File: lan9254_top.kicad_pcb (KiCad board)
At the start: 4 copper layers, 60 x 100 mm, 100 parts, among them J1 BEL_0845_2G1T_H5, J2 BNC, J3 BNC, SW1 SW_DIP_x08, U1 lan9254, U2 74LVC1G06, U3 74LVC1G06, U4 74LVC1G06, U5 PCA9306, U6 74LVC1G06, U7 74LVC2T45DC, U8 24AA0x, U9 74LVC2T45DC, X1 FNETHE025

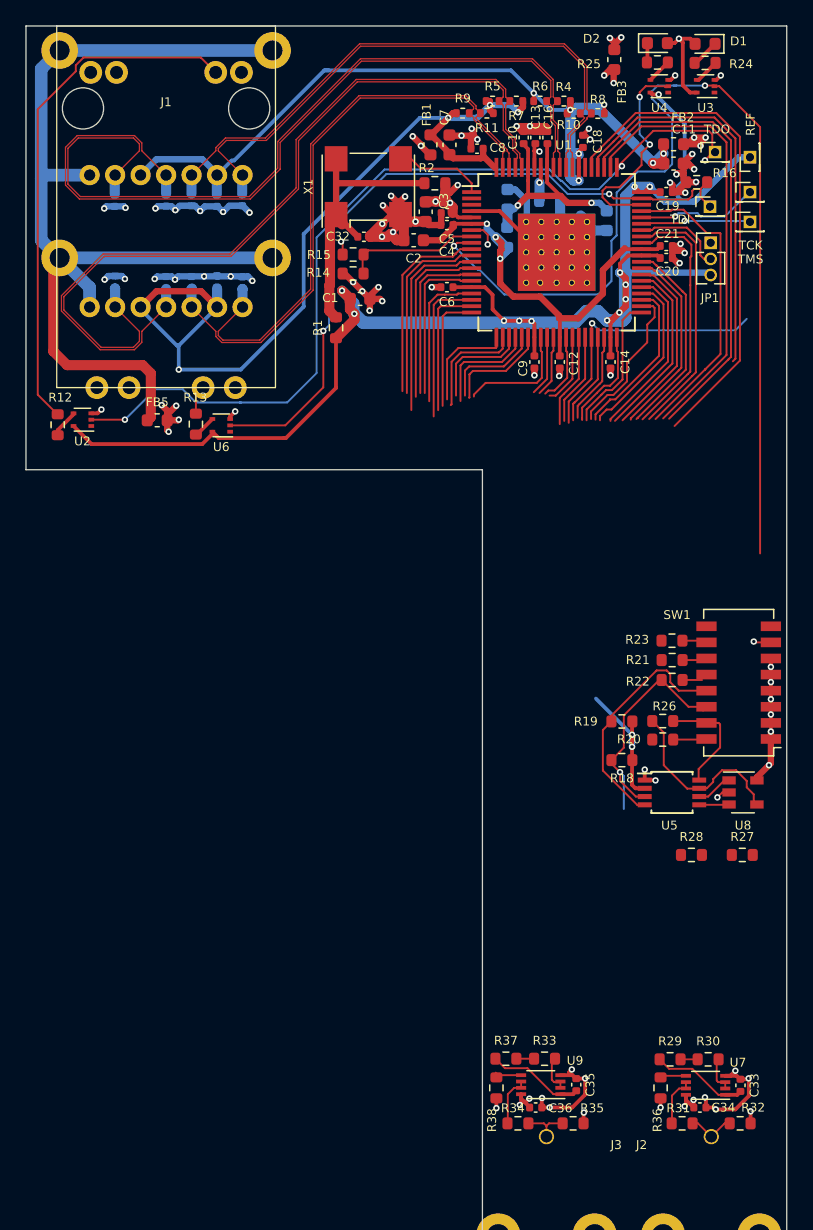
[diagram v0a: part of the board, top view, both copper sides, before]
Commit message: reannotated for merging with te0715 development board
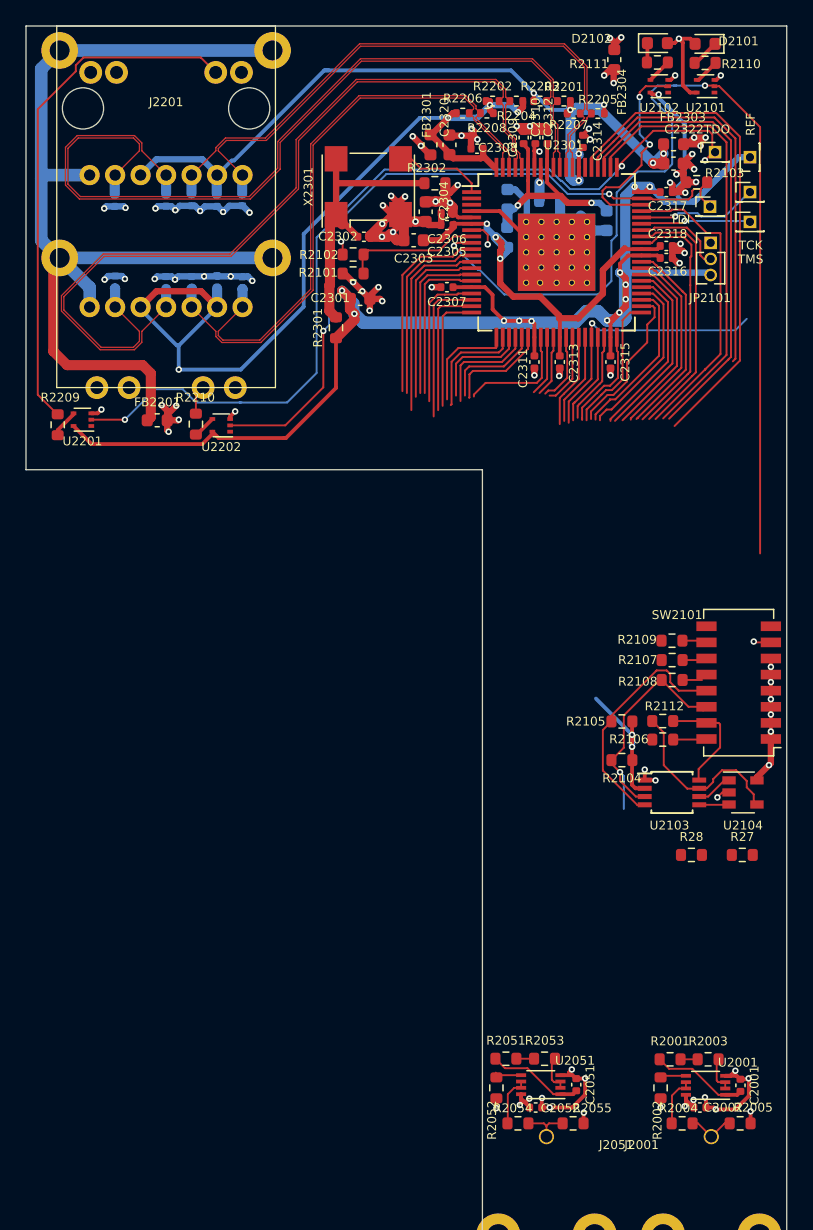
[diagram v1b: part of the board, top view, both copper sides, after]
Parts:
- renumbered C33 to C2001, C34 to C2002, C35 to C2051, C36 to C2052, C22 to C2201, C23 to C2202, C24 to C2203, C25 to C2204, C26 to C2205, C27 to C2206, C28 to C2207, C29 to C2208, C30 to C2209, C31 to C2210, C1 to C2301, C32 to C2302, C2 to C2303, C3 to C2304, C4 to C2305, C5 to C2306, C6 to C2307, C8 to C2308, C10 to C2309, C13 to C2310, C9 to C2311, C16 to C2312, C12 to C2313, C18 to C2314, C14 to C2315, C20 to C2316, C19 to C2317, C21 to C2318, C15 to C2319, C7 to C2320, C17 to C2321, C11 to C2322, D1 to D2101, D2 to D2102, FB5 to FB2201, FB1 to FB2301, FB4 to FB2302, FB2 to FB2303, FB3 to FB2304, J2 to J2001, J3 to J2051, J1 to J2201, JP1 to JP2101, R29 to R2001, R36 to R2002, R30 to R2003, R31 to R2004, R32 to R2005, R37 to R2051, R38 to R2052, R33 to R2053, R34 to R2054, R35 to R2055, R14 to R2101, R15 to R2102, R16 to R2103, R18 to R2104, R19 to R2105, R20 to R2106, R21 to R2107, R22 to R2108, R23 to R2109, R24 to R2110, R25 to R2111, R26 to R2112, R4 to R2201, R5 to R2202, R6 to R2203, R7 to R2204, R8 to R2205, R9 to R2206, R10 to R2207, R11 to R2208, R12 to R2209, R13 to R2210, R1 to R2301, R2 to R2302, R3 to R2303, SW1 to SW2101, TP1 to TP2301, TP2 to TP2302, TP3 to TP2303, TP4 to TP2304, TP5 to TP2305, U7 to U2001, U9 to U2051, U3 to U2101, U4 to U2102, U5 to U2103, U8 to U2104, U2 to U2201, U6 to U2202, U1 to U2301, X1 to X2301

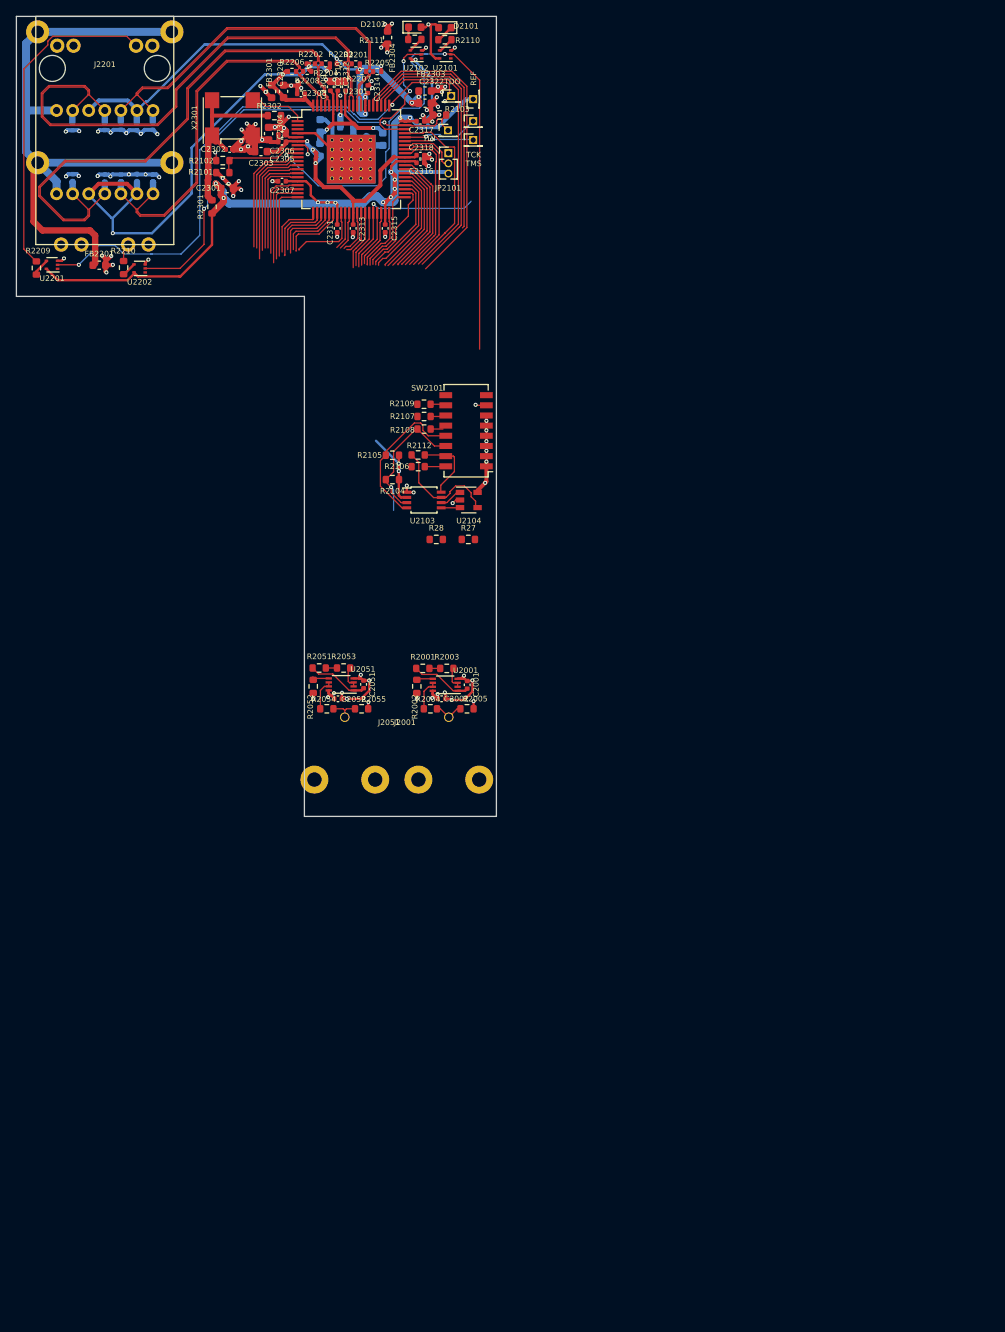
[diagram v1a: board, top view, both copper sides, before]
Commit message: moved PCB to not overlap with te0715 base board
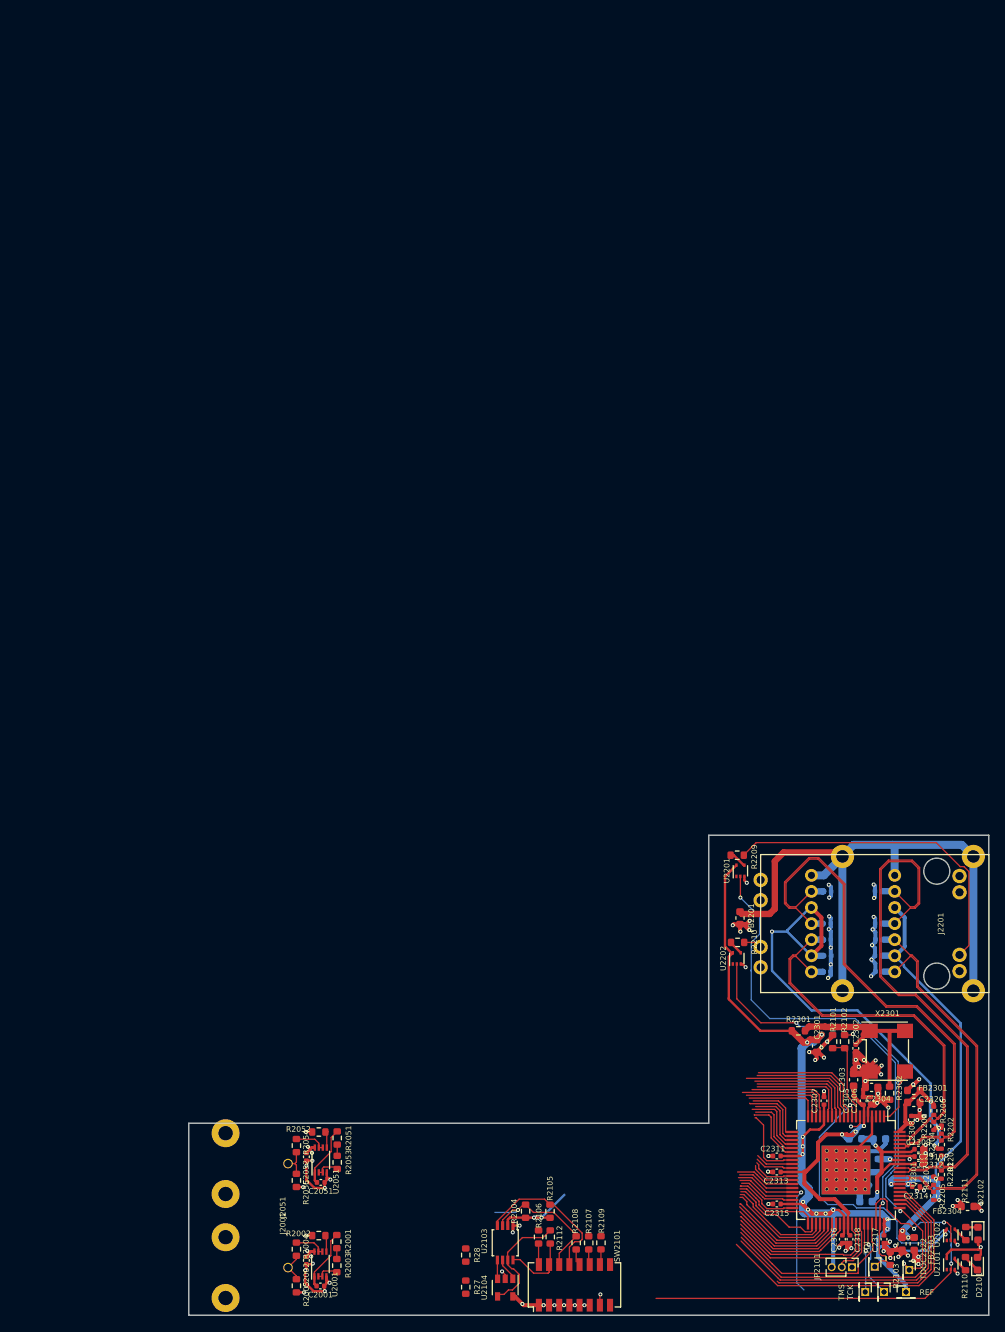
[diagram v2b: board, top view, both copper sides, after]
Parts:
- moved D2101 168.2 mm to (250.1, 195.9), turned to 90 degrees
- moved D2102 166.4 mm to (250.2, 192.2), turned to 270 degrees
- moved R2110 166.3 mm to (248.6, 195.9), turned to 270 degrees
- moved R2111 164.4 mm to (248.7, 192.2), turned to 270 degrees
- moved U2101 163.9 mm to (246.8, 195.9), turned to 90 degrees
- moved FB2304 163.1 mm to (248.9, 188.8), turned to 180 degrees
- moved U2102 162.0 mm to (246.8, 192.3), turned to 90 degrees
- moved TP2305 158.6 mm to (241.2, 199.4), turned to 0 degrees
- moved TP2301 157.5 mm to (241.6, 196.7), turned to 270 degrees
- moved R2201 157.0 mm to (245.6, 184.8), turned to 90 degrees
- moved R2205 156.8 mm to (244.7, 187.4), turned to 90 degrees
- moved FB2303 156.5 mm to (242.2, 193.4), turned to 90 degrees
- moved R2203 156.2 mm to (245.6, 182.9), turned to 270 degrees
- moved R2207 156.0 mm to (244.7, 185.6), turned to 270 degrees
- moved R2204 155.5 mm to (245.6, 181.0), turned to 90 degrees
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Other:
- board size 60 x 100 mm -> 100 x 60 mm

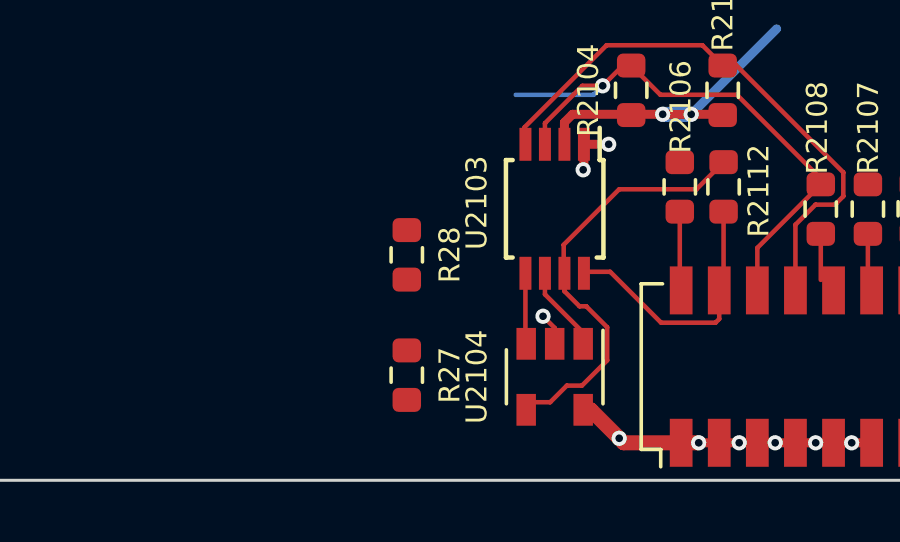
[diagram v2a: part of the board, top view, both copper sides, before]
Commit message: reannotated top-module and updated PCB (prior to merging with base-board)
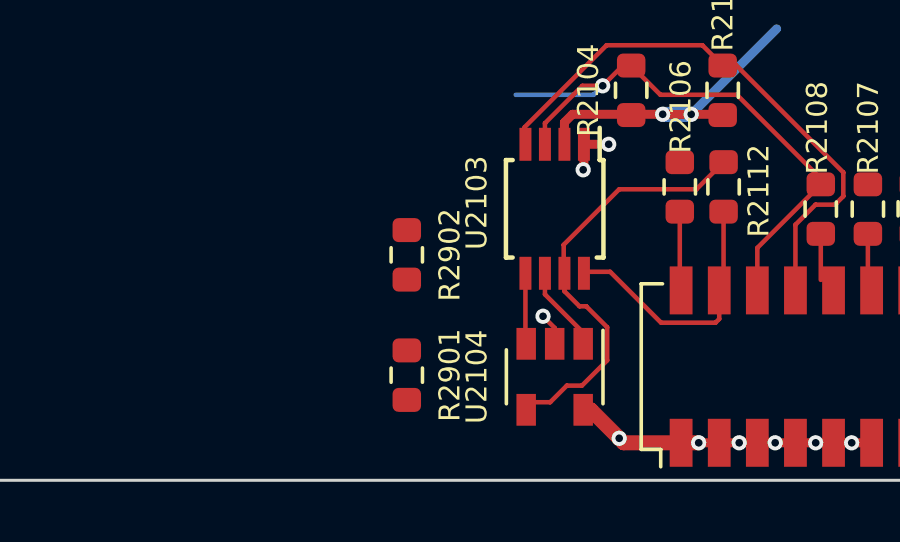
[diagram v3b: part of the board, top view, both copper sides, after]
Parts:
- renumbered R27 to R2901, R28 to R2902

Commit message: reduced default netclass clearance from 8mil to 6mil to match base-board setup
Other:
- net class Default: clearance 0.2 -> 0.1524
- rule trace_clearance: 0.2 -> 0.1524

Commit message: renamed diff-pair netclass diffp->diffp_ec due to mis-match with base-board setup
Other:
- net class diffp removed
- net class diffp_ec added: clearance 0.0889, trace_width 0.0889, via_dia 0.4, via_drill 0.2
